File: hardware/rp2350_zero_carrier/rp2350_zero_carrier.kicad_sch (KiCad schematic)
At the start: 8 parts, among them J1 RP2350-Zero_Header(20pin,pin番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, J2 USB-A_Host(Neltron_5075AR-04-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, SW1 1回路2接点スイッチ(3pin,NKK_115643,ON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, SW2 1回路2接点スイッチ(3pin,NKK_115643,ON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, SW3 1回路2接点スイッチ(3pin,NKK_115643,ON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

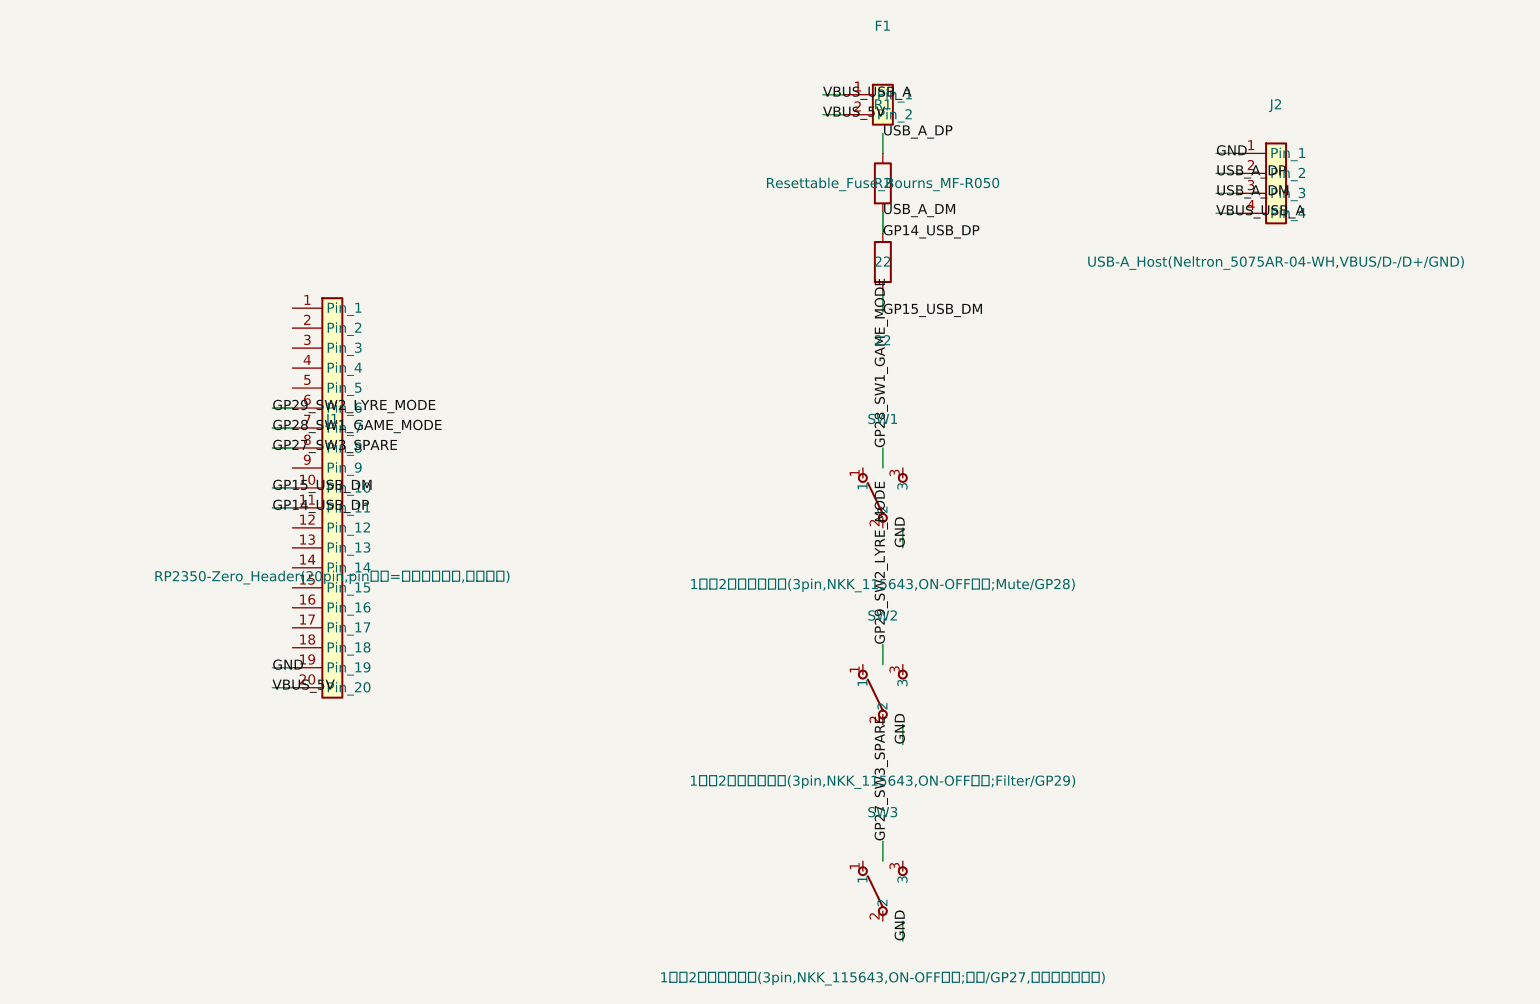
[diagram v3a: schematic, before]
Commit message: D+/D-をGP14/GP15からGP12/GP13へ復元(訂正の取り消し)
前回のGP14/GP15への変更はユーザーが誤った参考表に基づいて依頼したもので、
今回の正しいピン配置確認(左9/右8/下6=23pin)によりGP12/GP13が実在し
下辺で隣接することが判明したため取り消す。USB Host D+/D-はGP12/GP13に
戻り、旧基板(RP2350-USB-A)のconfig.h既定値と再び一致するため、ファーム
側のPIN_USB_HOST_DP変更は不要になった。

J1のネットラベルをfootprint側の新pin番号(pad4/5/6=GP29/28/27、
pad18/19=GP13/GP12)に合わせて再配置。R1/R2側のラベルもGP12/GP13へ
リネーム(定数変更なし)。BOMも合わせて更新。

Co-Authored-By: Claude Sonnet 5 <noreply@anthropic.com>
Claude-Session: https://claude.ai/code/session_01E7QH5gCzZj3tVha83XRuUt
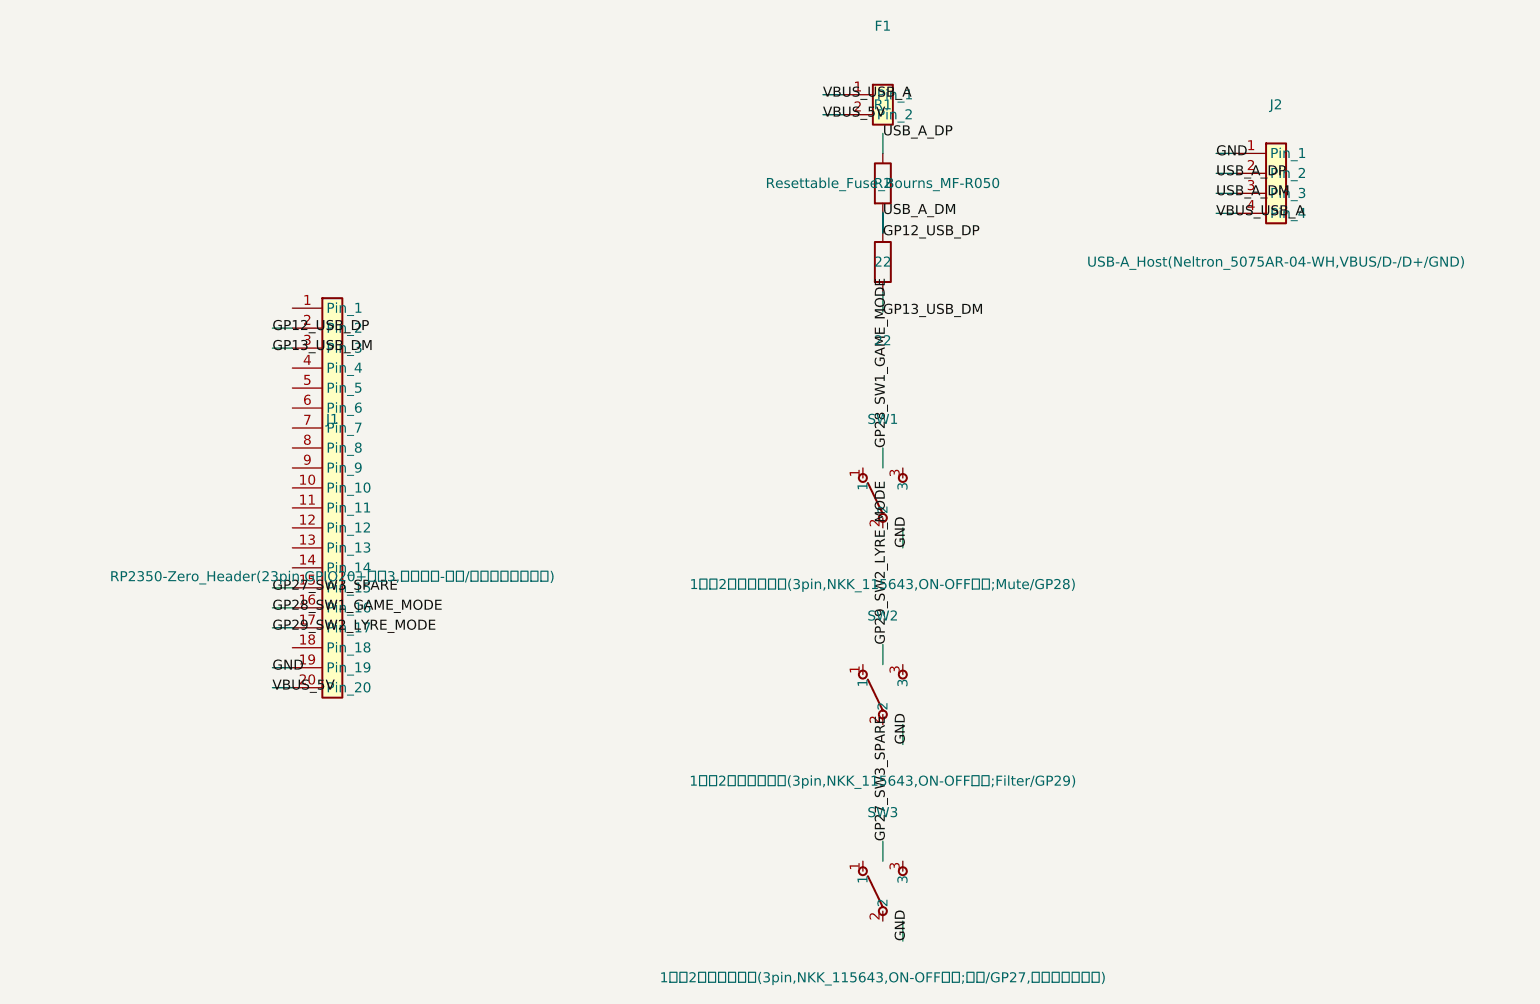
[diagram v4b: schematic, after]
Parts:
- J1: value RP2350-Zero_Header(20pin,pin番号=実物ピン番号,確定済み) -> RP2350-Zero_Header(23pin,GPIO20+電源3,確定済み-右列/下段は要目視確認); footprint rp2350_zero_carrier:RP2350_Zero_Header_20p -> rp2350_zero_carrier:RP2350_Zero_Header_23p
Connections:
- net GP27_SW3_SPARE: now also J1.15 (Pin_15); no longer J1.8 (Pin_8)
- net GP28_SW1_GAME_MODE: now also J1.16 (Pin_16); no longer J1.7 (Pin_7)
- net GP29_SW2_LYRE_MODE: now also J1.17 (Pin_17); no longer J1.6 (Pin_6)
- net GP12_USB_DP: now reaches J1.2 (Pin_2)
- net GP12_USB_DP: now also J2.3 (Pin_3), R1.2, R2.1
- net GP13_USB_DM: now reaches J1.3 (Pin_3)
- net GP13_USB_DM: now also R2.2
- removed net GP14_USB_DP: J1.11 (Pin_11), J2.3 (Pin_3), R1.2, R2.1
- net GP15_USB_DM: no longer names the net of J1.10 (Pin_10)
- net GP15_USB_DM: no longer R2.2
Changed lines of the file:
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@@
     (in_bom yes) (on_board yes) (dnp no) (fields_autoplaced yes)
     (property "Reference" "J1" (at 40 120 0) (effects (font (size 1.27 1.27))))
-    (property "Value" "RP2350-Zero_Header(20pin,pin番号=実物ピン番号,確定済み)" (at 40 140 0) (effects (font (size 1.27 1.27))))
-    (property "Footprint" "rp2350_zero_carrier:RP2350_Zero_Header_20p" (at 40 130 0) (effects (font (size 1.27 1.27)) hide))
+    (property "Value" "RP2350-Zero_Header(23pin,GPIO20+電源3,確定済み-右列/下段は要目視確認)" (at 40 140 0) (effects (font (size 1.27 1.27))))
+    (property "Footprint" "rp2350_zero_carrier:RP2350_Zero_Header_23p" (at 40 130 0) (effects (font (size 1.27 1.27)) hide))
     (property "Datasheet" "" (at 40 130 0) (effects (font (size 1.27 1.27)) hide))
     (pin "1")
@@
   (wire (pts (xy 34.92 154.13) (xy 32.38 154.13)) (stroke (width 0) (type default)))
   (wire (pts (xy 34.92 151.59) (xy 32.38 151.59)) (stroke (width 0) (type default)))
-  (wire (pts (xy 34.92 131.27) (xy 32.38 131.27)) (stroke (width 0) (type default)))
-  (wire (pts (xy 34.92 128.73) (xy 32.38 128.73)) (stroke (width 0) (type default)))
-  (wire (pts (xy 34.92 123.65) (xy 32.38 123.65)) (stroke (width 0) (type default)))
-  (wire (pts (xy 34.92 121.11) (xy 32.38 121.11)) (stroke (width 0) (type default)))
-  (wire (pts (xy 34.92 118.57) (xy 32.38 118.57)) (stroke (width 0) (type default)))
+  (wire (pts (xy 34.92 146.51) (xy 32.38 146.51)) (stroke (width 0) (type default)))
+  (wire (pts (xy 34.92 143.97) (xy 32.38 143.97)) (stroke (width 0) (type default)))
+  (wire (pts (xy 34.92 141.43) (xy 32.38 141.43)) (stroke (width 0) (type default)))
+  (wire (pts (xy 34.92 110.95) (xy 32.38 110.95)) (stroke (width 0) (type default)))
+  (wire (pts (xy 34.92 108.41) (xy 32.38 108.41)) (stroke (width 0) (type default)))
   (wire (pts (xy 110 93.81) (xy 110 96.35)) (stroke (width 0) (type default)))
   (wire (pts (xy 110 86.19) (xy 110 83.65)) (stroke (width 0) (type default)))
@@
   (label "VBUS_5V" (at 32.38 154.13 0) (effects (font (size 1.27 1.27)) (justify left)))
   (label "GND" (at 32.38 151.59 0) (effects (font (size 1.27 1.27)) (justify left)))
-  (label "GP14_USB_DP" (at 32.38 131.27 0) (effects (font (size 1.27 1.27)) (justify left)))
-  (label "GP15_USB_DM" (at 32.38 128.73 0) (effects (font (size 1.27 1.27)) (justify left)))
-  (label "GP27_SW3_SPARE" (at 32.38 123.65 0) (effects (font (size 1.27 1.27)) (justify left)))
-  (label "GP28_SW1_GAME_MODE" (at 32.38 121.11 0) (effects (font (size 1.27 1.27)) (justify left)))
-  (label "GP29_SW2_LYRE_MODE" (at 32.38 118.57 0) (effects (font (size 1.27 1.27)) (justify left)))
-  (label "GP14_USB_DP" (at 110 96.35 0) (effects (font (size 1.27 1.27)) (justify left)))
+  (label "GP29_SW2_LYRE_MODE" (at 32.38 146.51 0) (effects (font (size 1.27 1.27)) (justify left)))
+  (label "GP28_SW1_GAME_MODE" (at 32.38 143.97 0) (effects (font (size 1.27 1.27)) (justify left)))
+  (label "GP27_SW3_SPARE" (at 32.38 141.43 0) (effects (font (size 1.27 1.27)) (justify left)))
+  (label "GP13_USB_DM" (at 32.38 110.95 0) (effects (font (size 1.27 1.27)) (justify left)))
+  (label "GP12_USB_DP" (at 32.38 108.41 0) (effects (font (size 1.27 1.27)) (justify left)))
+  (label "GP12_USB_DP" (at 110 96.35 0) (effects (font (size 1.27 1.27)) (justify left)))
   (label "USB_A_DP" (at 110 83.65 0) (effects (font (size 1.27 1.27)) (justify left)))
-  (label "GP15_USB_DM" (at 110 106.35 0) (effects (font (size 1.27 1.27)) (justify left)))
+  (label "GP13_USB_DM" (at 110 106.35 0) (effects (font (size 1.27 1.27)) (justify left)))
   (label "USB_A_DM" (at 110 93.65 0) (effects (font (size 1.27 1.27)) (justify left)))
   (label "VBUS_5V" (at 102.38 81.27 0) (effects (font (size 1.27 1.27)) (justify left)))
